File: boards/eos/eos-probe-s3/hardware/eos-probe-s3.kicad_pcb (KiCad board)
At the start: 2 copper layers, 62 x 30 mm, 58 parts, among them J1 USB-C, J2 Cortex Debug, J3 Target UART, Q1 2N7002, SW1 RESET, SW2 BOOT, U1 USBLC6-2SC6, U2 AP7361C-33, U3 ESP32-S3-WROOM-1-N8R2, U4 SN74LVC1T45, U5 SN74LVC1T45, U6 SN74LVC1T45, U7 SN74LVC1T45, U8 SN74LVC1T45, U9 SN74LVC1T45

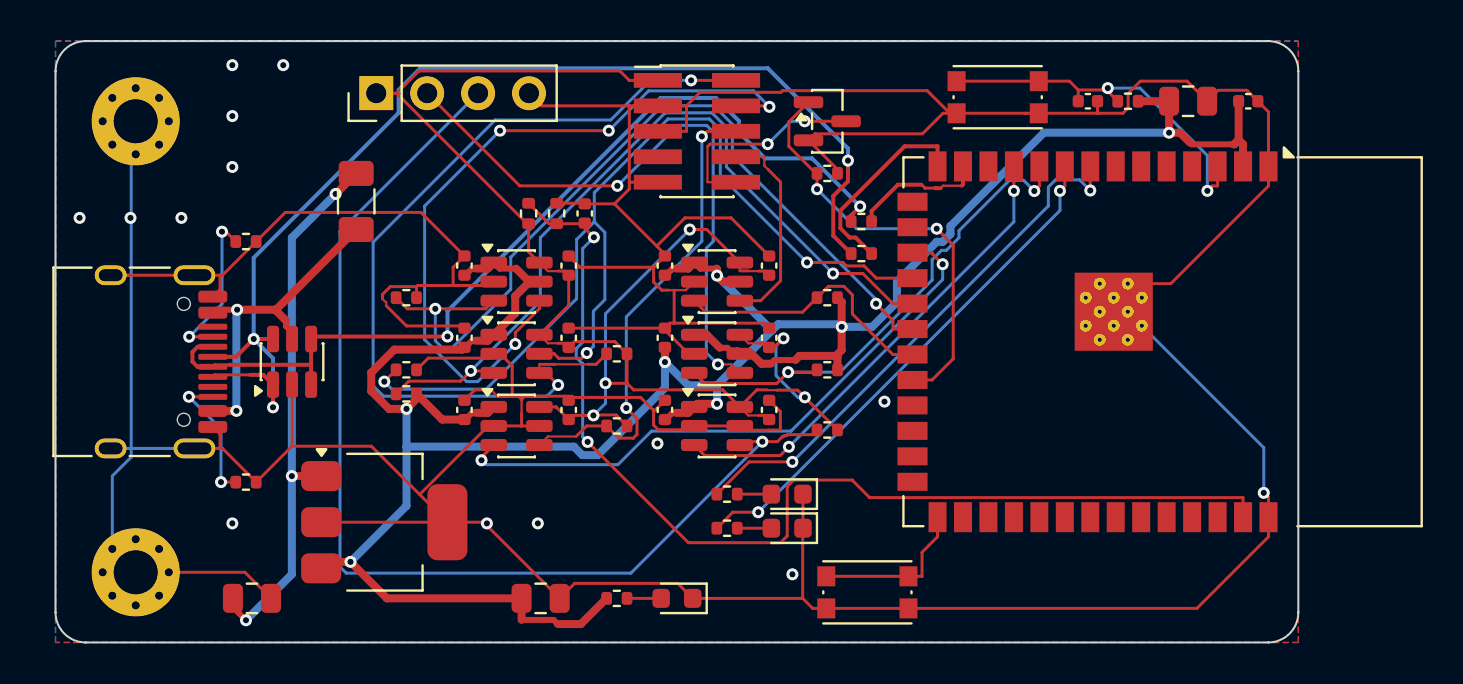
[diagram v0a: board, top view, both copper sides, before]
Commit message: fix(boards): USB-C receptacles at HRO's recommended edge distance
Each HRO TYPE-C-31-M-12 now sits with its footprint origin 3.19 mm from the
board edge it faces (design.USB_C_EDGE). HRO's "RECOMMEND P.C.B LAYOUT" draws
the PCB edge 5.79 mm from the locating pegs, which are 2.60 mm behind the
origin. At the old 3.8 mm the shell's face was 0.15 mm behind the edge, so a
plug's overmold could meet the board before the plug seated; the shell now
stands about 0.46 mm proud of it.

EoS Learn RP2350, EoS Probe S3 and EoS CM5 Base are moved and rebuilt: all
three report ERC 0, DRC errors 0, unconnected 0, schematic parity 0, with the
same DRC warnings as before (4, 4 and 6). On EoS CM5 Base, GPIO2 (the
header's SDA, CM5 pin 58) is now a priority route: after the move the
autorouter boxed its pad in twice, also with 100 passes.

UsbCEdgeTest checks every board's receptacles against the constant, within
the drawing's 0.05 mm tolerance. It fails for the old 3.8 mm placement.

Found in the independent review of a later board (EoS TM4C123 Board, M1).
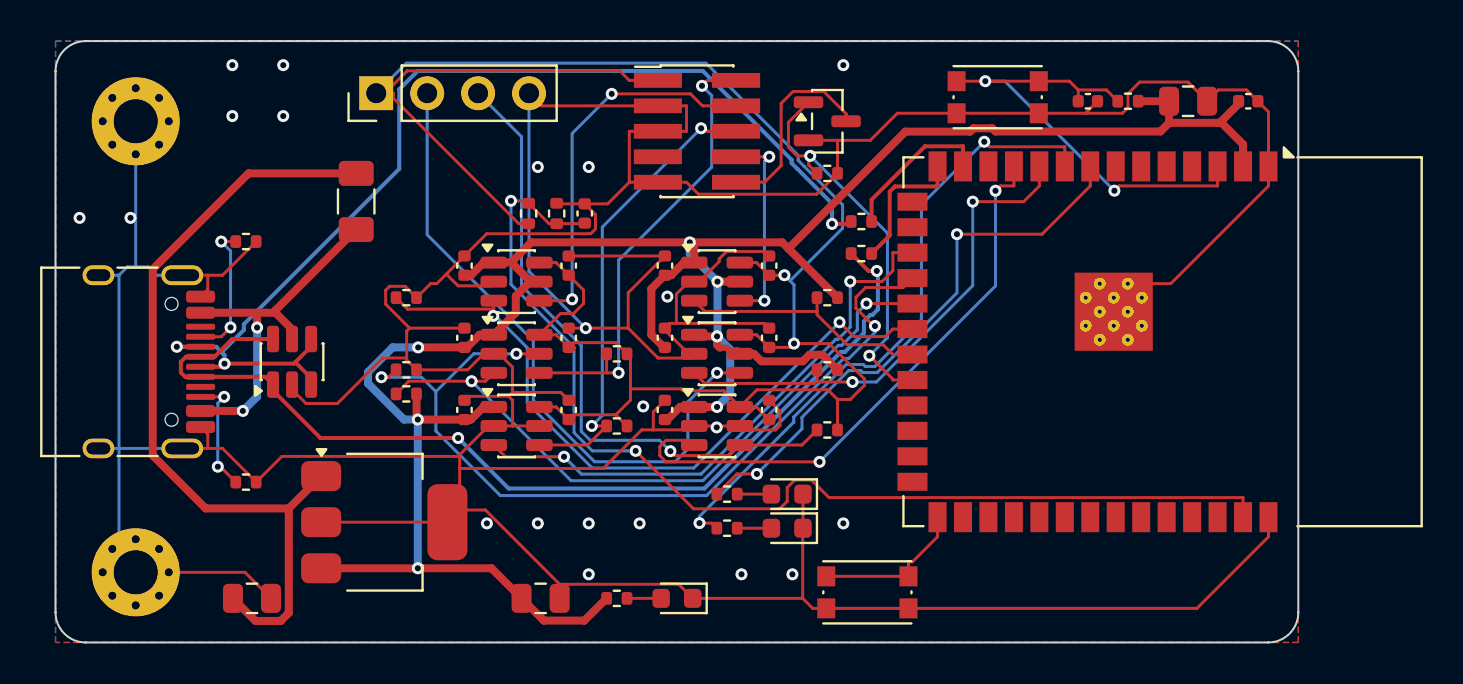
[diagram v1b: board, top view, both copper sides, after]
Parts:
- moved J1 0.61 mm to (3.19, 16.0)
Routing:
- net /VTREF: track 80.8 -> 106.0 mm, vias 5 -> 2
- net /T_UART_RX: track 54.6 -> 31.8 mm
- net /T_SWDIO: track 43.5 -> 23.2 mm
- net /T_SWCLK: track 37.1 -> 19.2 mm, vias 4 -> 2
- net +5V: track 27.4 -> 40.2 mm, vias 3 -> 0
- net /USB_D-: track 46.6 -> 55.5 mm, vias 2 -> 3
- net /SWCLK_A: track 42.6 -> 35.0 mm
- net +3V3: track 131.7 -> 124.7 mm
- net /USB_D+: track 57.4 -> 50.6 mm, vias 3 -> 2
- net /SWDIO_A: track 39.7 -> 33.5 mm
- net /SWDIO_DIR: track 49.8 -> 43.8 mm
- net /LED_ACT: track 26.0 -> 32.0 mm
- net /UART_RX_A: track 23.8 -> 29.7 mm
- net /EN: track 18.8 -> 23.9 mm
- net /ESP_D+: track 10.1 -> 6.96 mm
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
